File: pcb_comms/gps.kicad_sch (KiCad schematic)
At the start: 21 parts, among them J3 Conn_Coaxial, U1 MAX-M10M-00B

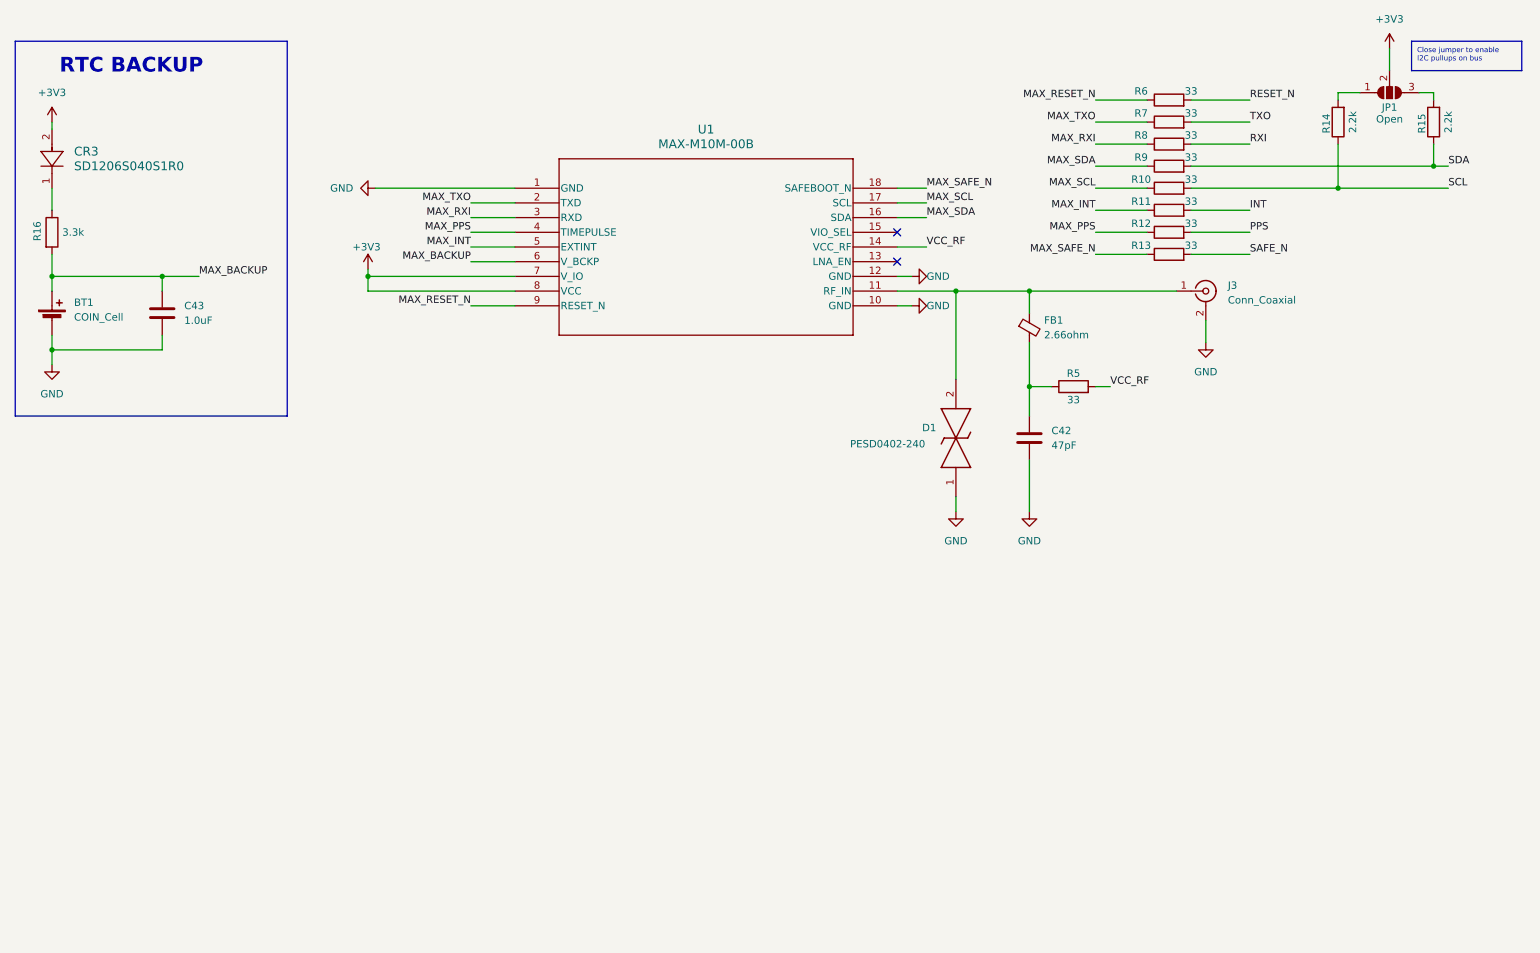
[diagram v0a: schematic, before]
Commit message: Add external circuit for gps
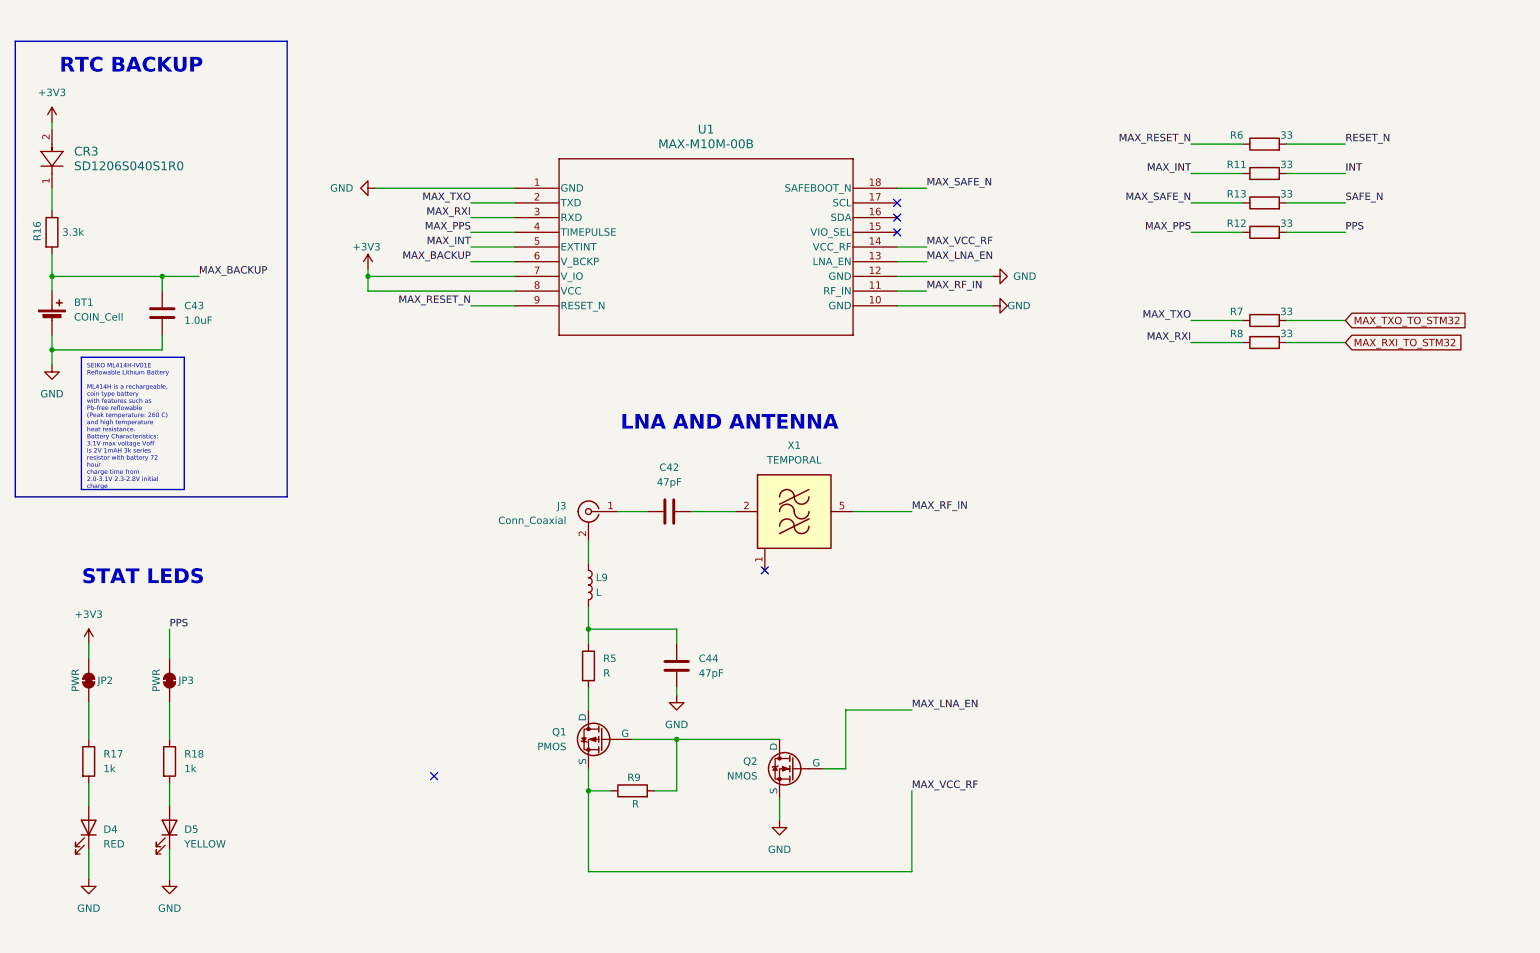
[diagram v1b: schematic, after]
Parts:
- removed D1: PESD0402-240, DIONC1005X43N, symbol ESD_PROTECTION_DIODE_PESD0402-240:PESD0402-240
- removed FB1: 2.66ohm, symbol Device:FerriteBead_Small
- removed JP1: Open, symbol Jumper:SolderJumper_3_Open
- removed R10: 33, symbol Device:R
- removed R14, R15: 2.2k, symbol Device:R
- added C44: 47pF, symbol Device:C
- added D4: RED, symbol Device:LED
- added D5: YELLOW, symbol Device:LED
- added JP2, JP3: PWR, symbol Jumper:SolderJumper_2_Bridged
- added L9: L, symbol Device:L
- added Q1: PMOS, symbol Simulation_SPICE:PMOS
- added Q2: NMOS, symbol Simulation_SPICE:NMOS
- added R17, R18: 1k, symbol Device:R
- added X1: TEMPORAL, Filter:Filter_SAW_Epcos_DCC6C_3x3mm, symbol RF_Filter:B3715
- R5, R9: value 33 -> R
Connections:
- net +3V3: now also JP2.2 (B)
- net GND: now also C44.1, D4.1 (K), D5.1 (K), Q2.3 (S); no longer C42.2, J3.2 (Ext)
- net PPS: now also JP3.2 (B)
- net at J3.1 (In): now also C42.1; no longer U1.11 (RF_IN)
- net at R5.1: now also C44.2, L9.2; no longer C42.1
- net MAX_LNA_EN: now reaches U1.13 (LNA_EN)
- net MAX_LNA_EN: now also Q2.2 (G)
- net MAX_SCL: no longer names the net of U1.17 (SCL)
- net MAX_SDA: no longer names the net of U1.16 (SDA)
- net MAX_SDA: no longer R9.1
- net RXI renamed MAX_RXI_TO_STM32
- net SDA: no longer names the net of R9.2
- net SDA: now also Q1.2 (G), Q2.1 (D)
- net TXO renamed MAX_TXO_TO_STM32
- net VCC_RF: no longer names the net of R5.2
- net VCC_RF: now also Q1.1 (D); no longer U1.14 (VCC_RF)
- new net: D5.2 (A), R18.2
- new net: C42.2, X1.2 (IN)
- new net: JP2.1 (A), R17.1
- new net: D4.2 (A), R17.2
- new net: JP3.1 (A), R18.1
- new net: J3.2 (Ext), L9.1
- new net: X1.1 (GND), X1.3 (GND), X1.4 (GND), X1.6 (GND)
- new net MAX_RF_IN: U1.11 (RF_IN), X1.5 (OUT)
- new net MAX_VCC_RF: Q1.3 (S), R9.1, U1.14 (VCC_RF)
- no-connect marks 2 -> 5
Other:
- note added: "LNA AND ANTENNA"
- note added: "STAT LEDS"
- moved on the sheet: C42, J3, R11, R12, R13, R6, R7, R8

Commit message: Update GPS to pasive antenna
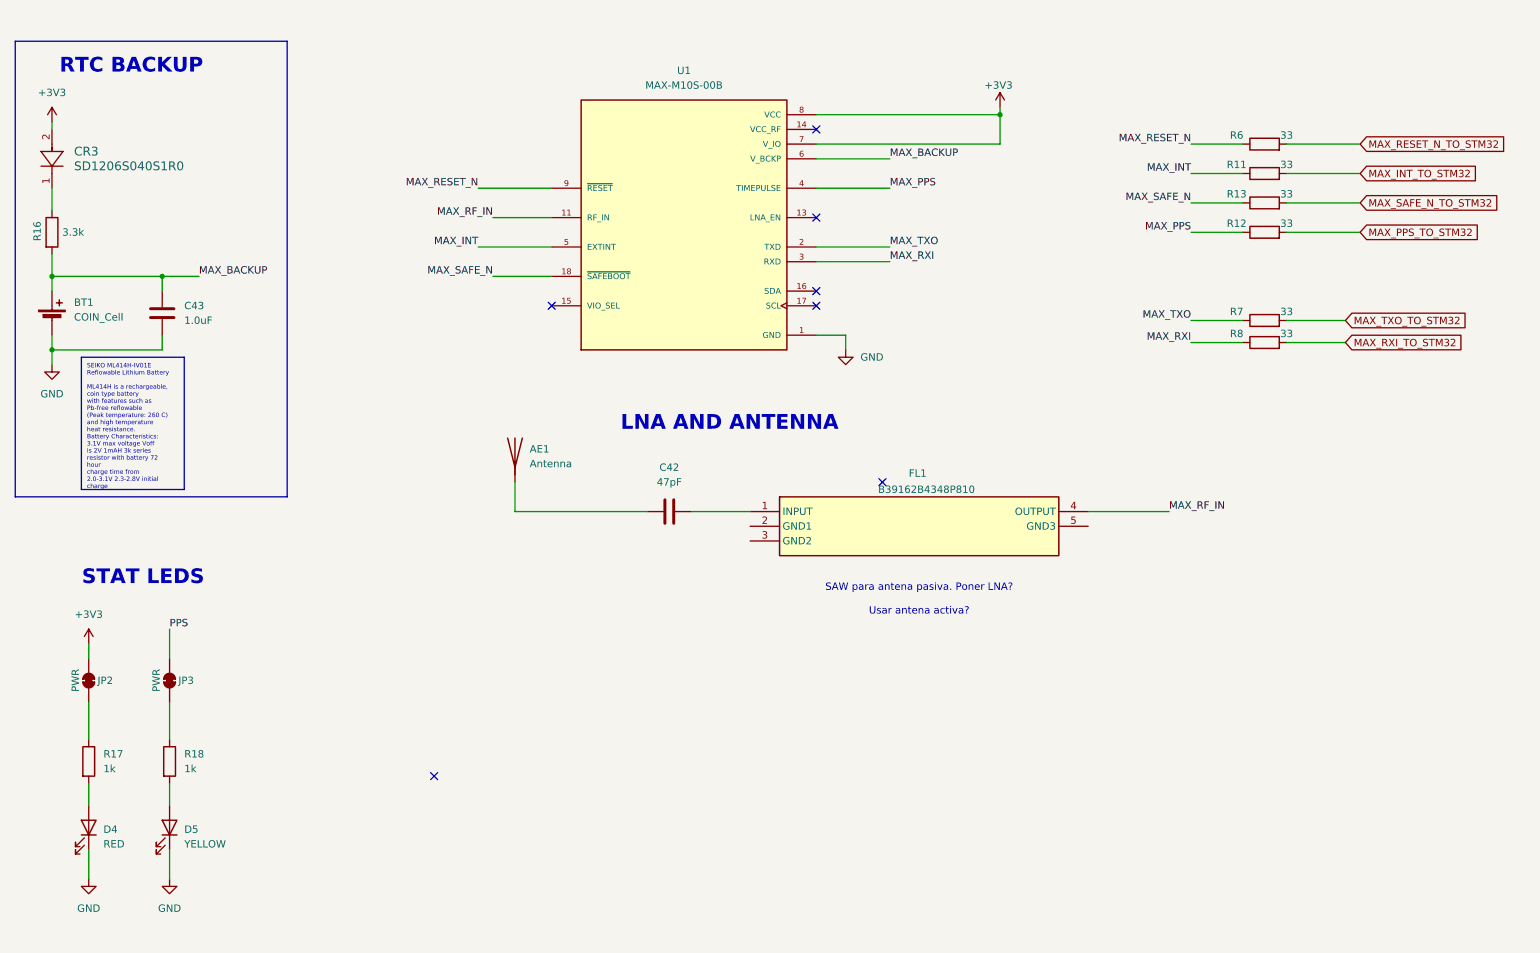
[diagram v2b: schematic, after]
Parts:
- removed C44: 47pF, symbol Device:C
- removed J3: Conn_Coaxial, symbol Connector:Conn_Coaxial
- removed L9: L, symbol Device:L
- removed Q1: PMOS, symbol Simulation_SPICE:PMOS
- removed Q2: NMOS, symbol Simulation_SPICE:NMOS
- removed R5, R9: R, symbol Device:R
- removed U1: MAX-M10M-00B, MOD18_MAX-M10M_UBL, symbol GPS_MAX_M10S:MAX-M10M-00B
- removed X1: TEMPORAL, Filter:Filter_SAW_Epcos_DCC6C_3x3mm, symbol RF_Filter:B3715
- added AE1: Antenna, symbol Device:Antenna
- added FL1: B39162B4348P810, B39162B4348P810, symbol GPS_SAW_FILTER_B39162B4348P810:B39162B4348P810
- added U1: MAX-M10S-00B, symbol MAX-M10S-00B:MAX-M10S-00B
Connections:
- net +3V3: now also U1.7 (V_IO), U1.8 (VCC)
- net GND: now also U1.1 (GND), U1.10 (GND), U1.12 (GND)
- net MAX_BACKUP: now also U1.6 (V_BCKP)
- net MAX_INT: now also U1.5 (EXTINT)
- net MAX_PPS: now also U1.4 (TIMEPULSE)
- net MAX_RESET_N: now also U1.9 (~{RESET})
- net MAX_RF_IN: now also FL1.4 (OUTPUT), U1.11 (RF_IN)
- net MAX_RXI: now also U1.3 (RXD)
- net MAX_SAFE_N: now also U1.18 (~{SAFEBOOT})
- net MAX_TXO: now also U1.2 (TXD)
- net PPS: no longer R12.2
- net at C42.1: now also AE1.1 (A)
- net at C42.2: now also FL1.1 (INPUT)
- net INT renamed MAX_INT_TO_STM32
- net RESET_N renamed MAX_RESET_N_TO_STM32
- net SAFE_N renamed MAX_SAFE_N_TO_STM32
- new net MAX_PPS_TO_STM32: R12.2
- no-connect marks 5 -> 7
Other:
- note added: "SAW para antena pasiva. Poner LNA? Usar antena activa?"

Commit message: Update GPS
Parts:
- removed JP2: PWR, symbol Jumper:SolderJumper_2_Bridged
- added D1: PESD0402-140, DIONC1005X43N, symbol ESD_PROTECTION_DIODE_PESD0402-140:PESD0402-140
- added FB1: 2.66 Ohms, symbol Device:FerriteBead_Small
- added R5: 330, symbol Device:R
- CR3: value SD1206S040S1R0 -> CUS10S30,H3F; footprint SD1206_AVX -> (none)
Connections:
- net PPS is gone; now on net MAX_PPS_TO_STM32: JP3.2 (B)
- net +3V3: now also R17.1
- net GND: now also C42.1, FL1.2 (GND1), FL1.3 (GND2), FL1.5 (GND3), D1.2
- net at AE1.1 (A): now also FL1.1 (INPUT), D1.1, FB1.1; no longer C42.1
- net at C42.2: now also FB1.2, R5.1; no longer FL1.1 (INPUT)
- net MAX_VCC_RF: now reaches U1.14 (VCC_RF)
- net MAX_VCC_RF: now also R5.2
- no-connect marks 7 -> 5
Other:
- note added: "FILTRO SAW AND ANTENNA"
- note added: "GPS MAX AND CONNS"
- note removed: "LNA AND ANTENNA"
- note removed: "SAW para antena pasiva. Poner LNA? Usar antena activa?"
- moved on the sheet: AE1, C42, FL1, R11, R12, R13, R6, R7, R8
